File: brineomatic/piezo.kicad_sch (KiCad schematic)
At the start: 3 parts, among them Q2 AO3400A

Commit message: kicad v9 and updated todo.
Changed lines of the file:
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@@
 (kicad_sch
-	(version 20231120)
+	(version 20250114)
 	(generator "eeschema")
-	(generator_version "8.0")
+	(generator_version "9.0")
 	(paper "A4")
+	(rectangle
+		(start 110.49 58.42)
+		(end 168.91 111.76)
+		(stroke
+			(width 0)
+			(type default)
+		)
+		(fill
+			(type none)
+		)
+	)
+	(text "Piezo Buzzer"
+		(exclude_from_sim no)
+		(at 111.76 61.468 0)
+		(effects
+			(font
+				(size 1.27 1.27)
+			)
+			(justify left bottom)
+		)
+	)
 	(wire
 		(pts
@@
 		)
 	)
-	(rectangle
-		(start 110.49 58.42)
-		(end 168.91 111.76)
-		(stroke
-			(width 0)
-			(type default)
-		)
-		(fill
-			(type none)
-		)
-	)
-	(text "Piezo Buzzer"
-		(exclude_from_sim no)
-		(at 111.76 61.468 0)
-		(effects
-			(font
-				(size 1.27 1.27)
-			)
-			(justify left bottom)
-		)
-	)
 	(hierarchical_label "PIEZO"
 		(shape input)
 		(at 123.19 93.98 180)
-		(fields_autoplaced yes)
 		(effects
 			(font

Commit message: worked on schematic and layout a bit more.
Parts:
- R2: footprint Resistor_SMD:R_0805_2012Metric_Pad1.20x1.40mm_HandSolder -> Resistor_SMD:R_0603_1608Metric
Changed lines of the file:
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@@
 			)
 		)
-		(property "Footprint" "Resistor_SMD:R_0805_2012Metric_Pad1.20x1.40mm_HandSolder"
+		(property "Footprint" "Resistor_SMD:R_0603_1608Metric"
 			(at 129.54 93.98 0)
 			(effects

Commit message: lots of progress on Rev B
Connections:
- net GNDD renamed GND
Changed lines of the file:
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@@
+	)
+	(symbol
+		(lib_id "power:GND")
+		(at 143.51 102.87 0)
+		(unit 1)
+		(exclude_from_sim no)
+		(in_bom yes)
+		(on_board yes)
+		(dnp no)
+		(fields_autoplaced yes)
+		(property "Reference" "#PWR010"
+			(at 143.51 109.22 0)
+			(effects
+				(font
+					(size 1.27 1.27)
+				)
+				(hide yes)
+			)
+		)
+		(property "Value" "GND"
+			(at 143.51 107.95 0)
+			(effects
+				(font
+					(size 1.27 1.27)
+				)
+			)
+		)
+		(property "Footprint" ""
+			(at 143.51 102.87 0)
+			(effects
+				(font
+					(size 1.27 1.27)
+				)
+				(hide yes)
+			)
+		)
+		(property "Datasheet" ""
+			(at 143.51 102.87 0)
+			(effects
+				(font
+					(size 1.27 1.27)
+				)
+				(hide yes)
+			)
+		)
+		(property "Description" "Power symbol creates a global label with name \"GND\" , ground"
+			(at 143.51 102.87 0)
+			(effects
+				(font
+					(size 1.27 1.27)
+				)
+				(hide yes)
+			)
+		)
+		(pin "1"
+		)
+		(instances
+			(project ""
+				(path "/96477ae2-ef08-48f3-8dd4-fe4478541f68/8bb47731-29fc-477e-bfb2-3ccc154aa914"
+					(reference "#PWR010")
+					(unit 1)
+				)
+			)
+		)
 	)
 	(symbol
@@
 					(unit 1)
 				)
-			)
-		)
-	)
-	(symbol
-		(lib_id "power:GNDD")
-		(at 143.51 102.87 0)
-		(unit 1)
-		(exclude_from_sim no)
-		(in_bom yes)
-		(on_board yes)
-		(dnp no)
-		(fields_autoplaced yes)
-		(property "Reference" "#PWR038"
-			(at 143.51 109.22 0)
-			(effects
-				(font
-					(size 1.27 1.27)
-				)
-				(hide yes)
-			)
-		)
-		(property "Value" "GNDD"
-			(at 143.51 106.68 0)
-			(effects
-				(font
-					(size 1.27 1.27)
-				)
-			)
-		)
-		(property "Footprint" ""
-			(at 143.51 102.87 0)
-			(effects
-				(font
-					(size 1.27 1.27)
-				)
-				(hide yes)
-			)
-		)
-		(property "Datasheet" ""
-			(at 143.51 102.87 0)
-			(effects
-				(font
-					(size 1.27 1.27)
-				)
-				(hide yes)
-			)
-		)
-		(property "Description" "Power symbol creates a global label with name \"GNDD\" , digital ground"
-			(at 143.51 102.87 0)
-			(effects
-				(font
-					(size 1.27 1.27)
-				)
-				(hide yes)
-			)
-		)
-		(pin "1"
-		)
-		(instances
-			(project "brineomatic"
-				(path "/96477ae2-ef08-48f3-8dd4-fe4478541f68/8bb47731-29fc-477e-bfb2-3ccc154aa914"
-					(reference "#PWR038")
-					(unit 1)
-				)

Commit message: tmc2209 driver schematic checked and laid out nicely.
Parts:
- renumbered R2 to R17
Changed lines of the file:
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@@
 		(dnp no)
 		(fields_autoplaced yes)
-		(property "Reference" "#PWR010"
+		(property "Reference" "#PWR023"
 			(at 143.51 69.85 0)
 			(effects
@@
 			(project "brineomatic"
 				(path "/96477ae2-ef08-48f3-8dd4-fe4478541f68/d9651726-ebc8-4cdb-a521-a43a3039a77a"
-					(reference "#PWR010")
+					(reference "#PWR023")
 					(unit 1)
 				)
@@
 		(dnp no)
 		(fields_autoplaced yes)
-		(property "Reference" "R2"
+		(property "Reference" "R17"
 			(at 129.54 87.63 90)
 			(effects
@@
 			(project "brineomatic"
 				(path "/96477ae2-ef08-48f3-8dd4-fe4478541f68/d9651726-ebc8-4cdb-a521-a43a3039a77a"
-					(reference "R2")
+					(reference "R17")
 					(unit 1)
 				)
@@
 		(dnp no)
 		(fields_autoplaced yes)
-		(property "Reference" "#PWR015"
+		(property "Reference" "#PWR024"
 			(at 143.51 109.22 0)
 			(effects
@@
 			(project "brineomatic"
 				(path "/96477ae2-ef08-48f3-8dd4-fe4478541f68/d9651726-ebc8-4cdb-a521-a43a3039a77a"
-					(reference "#PWR015")
-					(unit 1)
-				)
+					(reference "#PWR024")
+					(unit 1)
+				)

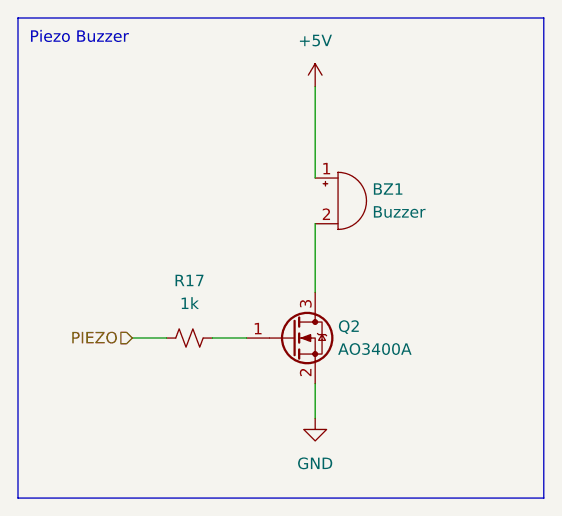
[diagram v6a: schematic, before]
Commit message: fully routed and erc/drc passed
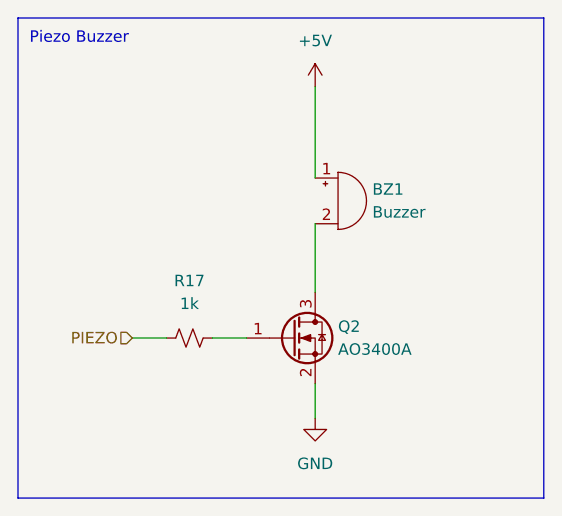
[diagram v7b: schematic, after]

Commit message: worked on bom for rev b prototype run
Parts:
- R17: LCSC C95781 -> (none)
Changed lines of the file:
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@@
 			)
 		)
-		(property "LCSC" "C95781"
+		(property "LCSC" ""
 			(at 129.54 93.98 0)
 			(effects
